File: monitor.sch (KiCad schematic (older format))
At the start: 26 parts, among them U1 LM317L, U2 AD8418, U3 CD4017, U4 TLC555

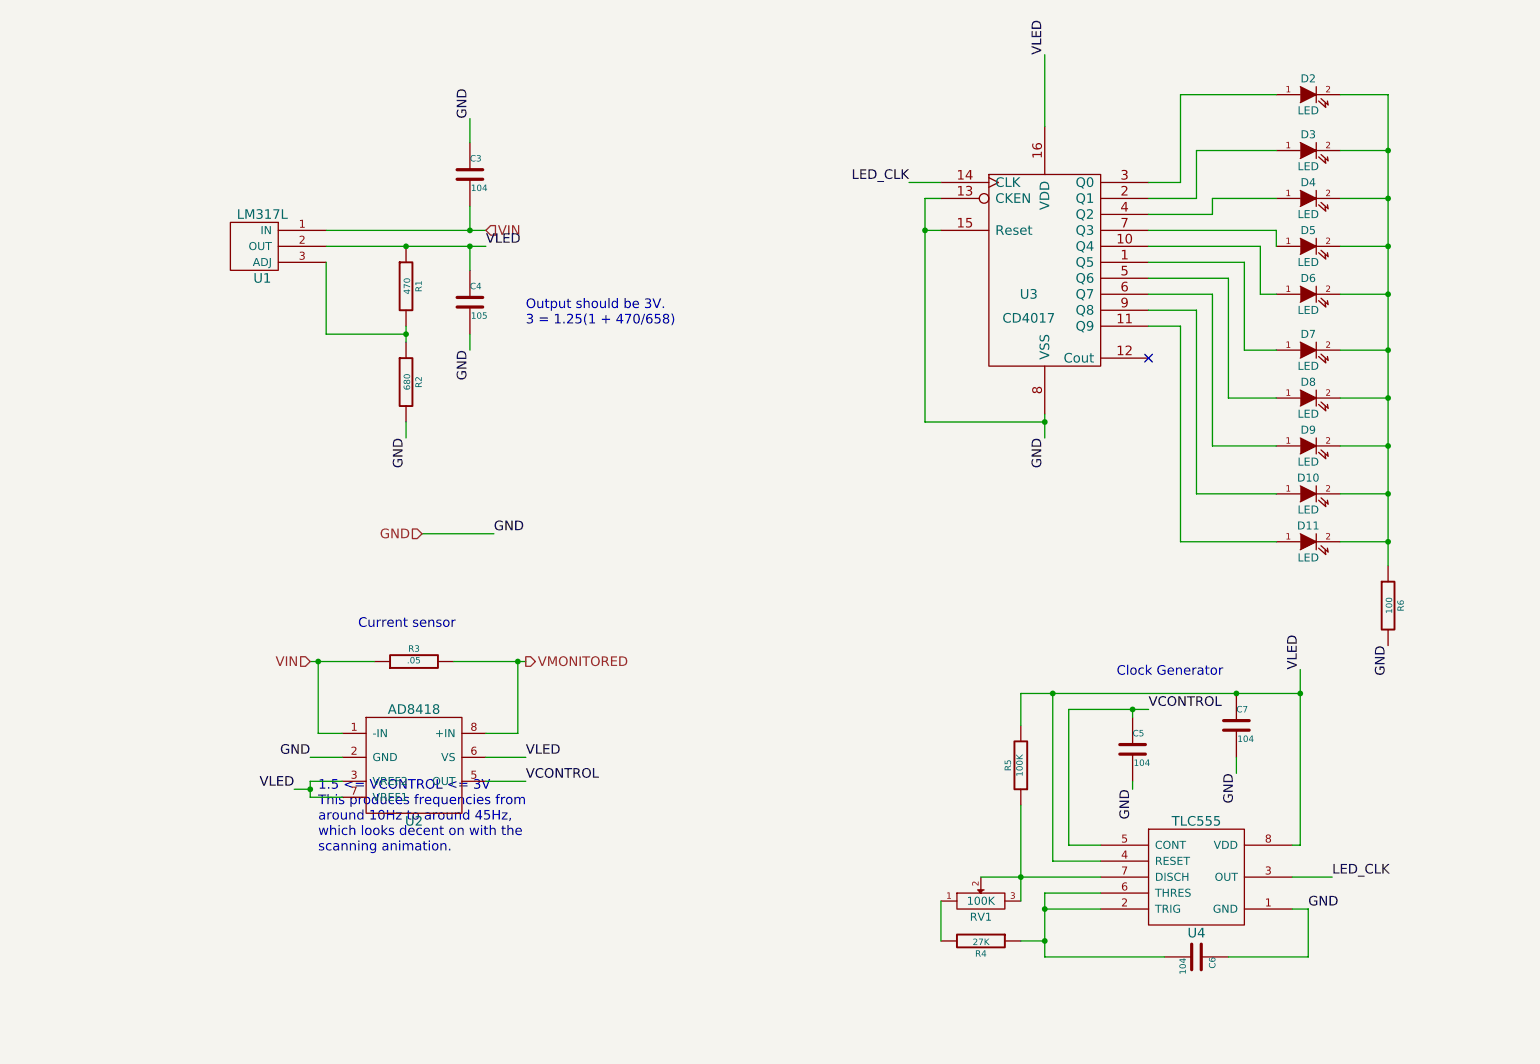
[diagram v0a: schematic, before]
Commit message: Rearranged, added a few things (look at long msg).
Renamed to power_supply (boring, but more professional).
Rearranged schematic to look somewhat organized.
Added more description.
Added Li-Ion charger circuit.
Added Phone charger output w/ adjustable resistors on data lines.
Added over voltage protection for phone charger and Li-Ion charger (cuts
	these two off at 5.1V.
Switched to terminal block for output.
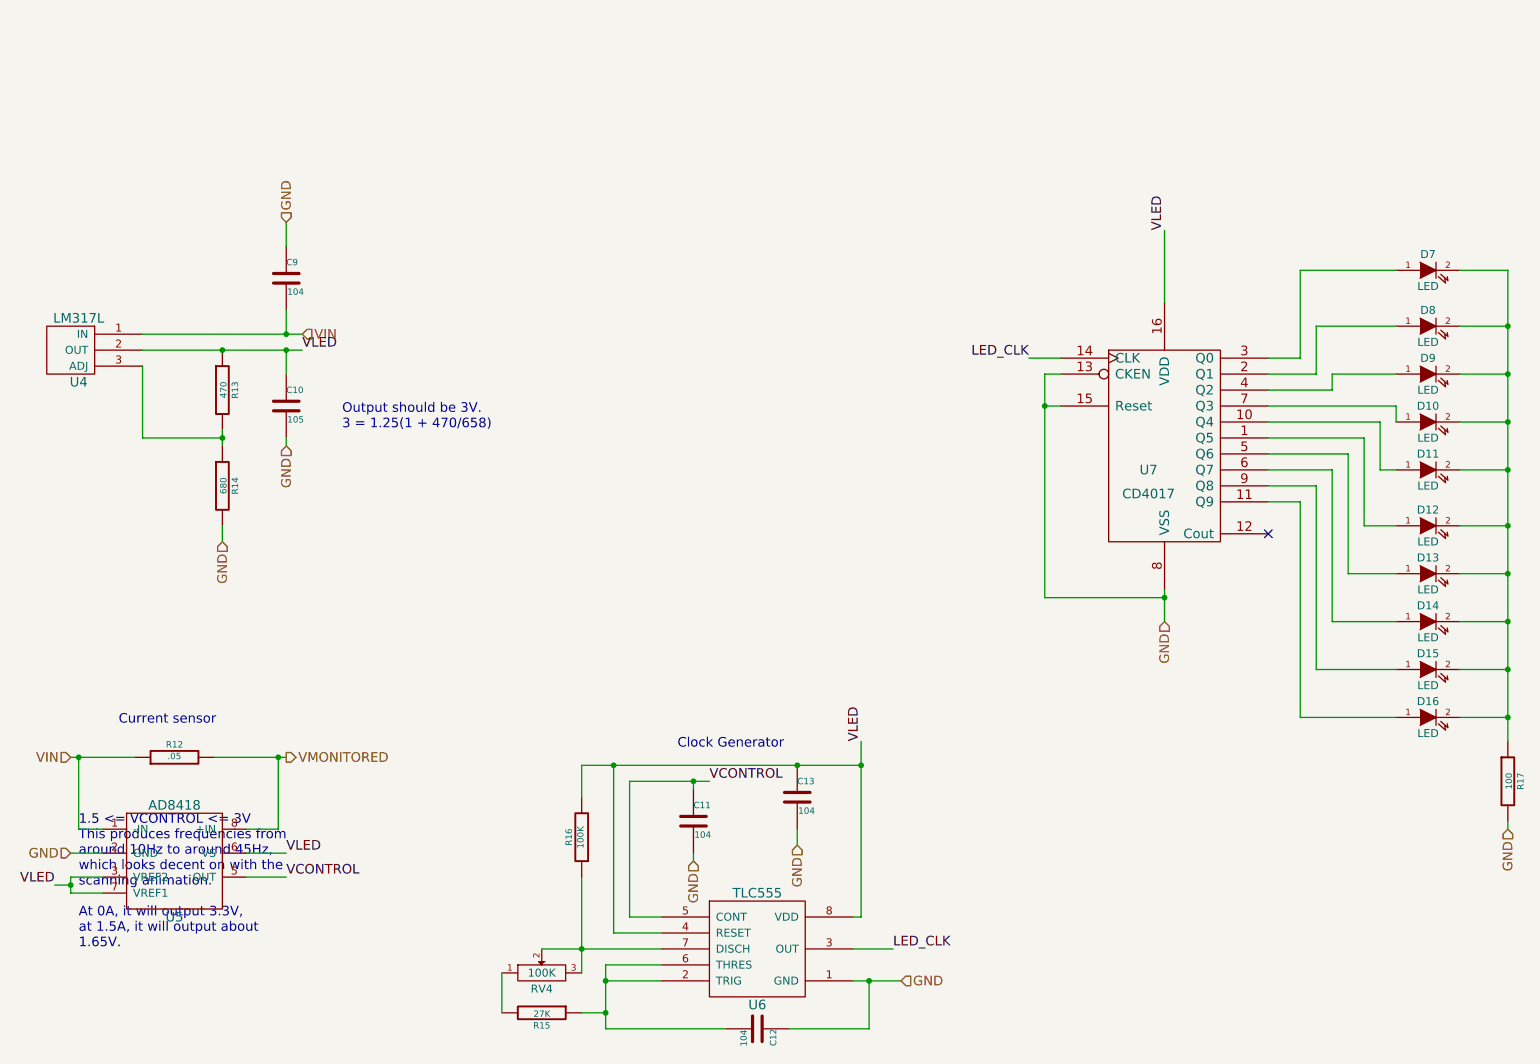
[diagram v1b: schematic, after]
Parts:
- renumbered C4 to C10, C5 to C11, C6 to C12, C7 to C13, C3 to C9, D5 to D10, D6 to D11, D7 to D12, D8 to D13, D9 to D14, D10 to D15, D11 to D16, D2 to D7, D3 to D8, D4 to D9, R3 to R12, R1 to R13, R2 to R14, R4 to R15, R5 to R16, R6 to R17, RV1 to RV4, U1 to U4, U2 to U5, U4 to U6, U3 to U7
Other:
- note added: "1.5 <= VCONTROL <= 3V\nThis produces frequencies from \naround 10Hz to around 45Hz, \nwhich looks decent on with the\nscanning animation.\n\nAt 0A, it will output 3.3V,\nat 1.5A, it will output about\n1.65V."
- note removed: "1.5 <= VCONTROL <= 3V\nThis produces frequencies from \naround 10Hz to around 45Hz, \nwhich looks decent on with the\nscanning animation."
- moved on the sheet: C10, C11, C12, C13, C9, D10, D11, D12, D13, D14, D15, D16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

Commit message: Updated from bob feedback
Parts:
- renumbered R12 to R14, R13 to R15, R14 to R16, R15 to R17, R16 to R18, R17 to R19
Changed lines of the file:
@@
 $EndComp
 $Comp
-L R R13
+L R R15
 U 1 1 532FC744
 P 2400 3100
-F 0 "R13" V 2480 3100 40  0000 C CNN
+F 0 "R15" V 2480 3100 40  0000 C CNN
 F 1 "470" V 2407 3101 40  0000 C CNN
 F 2 "~" V 2330 3100 30  0000 C CNN
@@
 $EndComp
 $Comp
-L R R14
+L R R16
 U 1 1 532FC74A
 P 2400 3700
-F 0 "R14" V 2480 3700 40  0000 C CNN
+F 0 "R16" V 2480 3700 40  0000 C CNN
 F 1 "680" V 2407 3701 40  0000 C CNN
 F 2 "~" V 2330 3700 30  0000 C CNN
@@
 $EndComp
 $Comp
-L R R12
+L R R14
 U 1 1 532FC800
 P 2100 5400
-F 0 "R12" V 2180 5400 40  0000 C CNN
+F 0 "R14" V 2180 5400 40  0000 C CNN
 F 1 ".05" V 2107 5401 40  0000 C CNN
 F 2 "~" V 2030 5400 30  0000 C CNN
@@
 $EndComp
 $Comp
-L R R16
+L R R18
 U 1 1 532FDE7B
 P 4650 5900
-F 0 "R16" V 4730 5900 40  0000 C CNN
+F 0 "R18" V 4730 5900 40  0000 C CNN
 F 1 "100K" V 4657 5901 40  0000 C CNN
 F 2 "~" V 4580 5900 30  0000 C CNN
@@
 $EndComp
 $Comp
-L R R15
+L R R17
 U 1 1 532FDE81
 P 4400 7000
-F 0 "R15" V 4480 7000 40  0000 C CNN
+F 0 "R17" V 4480 7000 40  0000 C CNN
 F 1 "27K" V 4407 7001 40  0000 C CNN
 F 2 "~" V 4330 7000 30  0000 C CNN
@@
 Clock Generator
 $Comp
-L R R17
+L R R19
 U 1 1 533055BA
 P 10450 5550
-F 0 "R17" V 10530 5550 40  0000 C CNN
+F 0 "R19" V 10530 5550 40  0000 C CNN
 F 1 "100" V 10457 5551 40  0000 C CNN
 F 2 "~" V 10380 5550 30  0000 C CNN

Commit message: Updating to new design
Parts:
- removed C10: 105, ~, symbol C
- removed C11, C12, C13, C9: 104, ~, symbol C
- removed D10, D11, D12, D13, D14, D15, D16, D7, D8, D9: LED, ~, symbol LED
- removed R15: 470, ~, symbol R
- removed R16: 680, ~, symbol R
- removed R17: 27K, ~, symbol R
- removed R18: 100K, ~, symbol R
- removed R19: 100, ~, symbol R
- removed RV4: 100K, ~, symbol POT
- removed U4: LM317L, symbol LM317L
- removed U6: TLC555, symbol TLC555
- removed U7: CD4017, symbol CD4017
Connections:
- no-connect marks 1 -> 0
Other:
- note removed: "Clock Generator"
- note removed: "Output should be 3V.\n3 = 1.25(1 + 470/658)"
- moved on the sheet: R14, U5
